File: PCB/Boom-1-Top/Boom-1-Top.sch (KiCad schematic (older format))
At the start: 983 parts, among them J1 DEBUG, J10 PIC_DEBUG, J11 PIC_DEBUG, J12 PIC_DEBUG, J13 PIC_DEBUG, J14 PIC_DEBUG, J15 USB_B_Micro, J16 SD_Card, J17 BT_DEBUG, J18 12V Supply, J19 3V3 Bypass, J2 MIDI IN, J20 5V Bypass, J21 Env +12V Supply, J22 Env -12V Supply, J23 OLEDConn, J3 MIDI OUT, J37 Osc1Conn, J38 Osc2Conn, J39 SubNoiseConn, J4 PIC_DEBUG, J40 FiltConn2, J41 EnvGenConn2, J42 EnvGenConn1, J43 FXConn1, J44 FiltConn1, J45 FXConn2, J46 EnvGenConn3, J5 PIC_DEBUG, J6 PIC_DEBUG, J7 PIC_DEBUG, J8 PIC_DEBUG, J9 PIC_DEBUG, Q1 AO3401A, Q2 AO3401A, SW1 Osc1SawEncoder, SW10 SubToOsc2FiltEncoder, SW11 Osc1ToOsc2FiltEncoder, SW12 Osc1FiltFreqEncoder, SW13 Osc2FiltFreqEncoder, SW14 SubFiltFreqEncoder, SW15 OscFiltEnvAttackEncoder, SW16 SubFiltEnvAttackEncoder, SW17 Osc1FiltResEncoder, SW18 Osc2FiltResEncoder, SW19 SubFiltResEncoder, SW2 Osc1SqrEncoder, SW20 OscFiltEnvDecayEncoder, SW21 SubFiltEnvDecayEncoder, SW22 OscFiltEnvSustainEncoder, SW23 SubFiltEnvSustainEncoder, SW24 Osc1DriveEncoder, SW25 Osc2DistortionEncoder, SW26 OscFiltEnvReleaseEncoder, SW27 SubFiltEnvReleaseEncoder, SW28 FXWetDryEncoder, SW29 SubAmpEnvAttackEncoder, SW3 Rotary_Encoder, SW30 OscAmpEnvAttackEncoder, SW31 FXControl1Encoder, SW32 SubAmpEnvDecayEncoder, SW33 OscAmpEnvDecayEncoder, SW34 FXControl2Encoder, SW35 SubAmpEnvSustainEncoder, SW36 OscAmpEnvSustainEncoder, SW37 FXControl3Encoder, SW38 FXFeedbackEncoder, SW39 SubAmpEnvReleaseEncoder, SW4 Rotary_Encoder_Switch, SW40 OscAmpEnvReleaseEncoder, SW41 Reset, SW42 SW_Push, SW43 Reset, SW44 SW_Push, SW45 SW_Push, SW46 SW_Push, SW47 SW_Push, SW48 SW_Push, SW49 SW_Push, SW5 Rotary_Encoder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

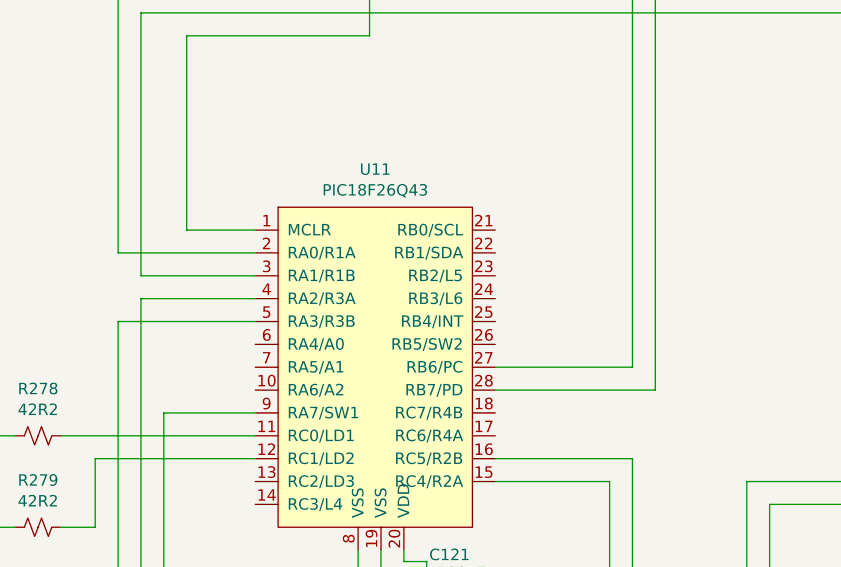
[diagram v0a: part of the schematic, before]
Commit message: U11 PIC i2c
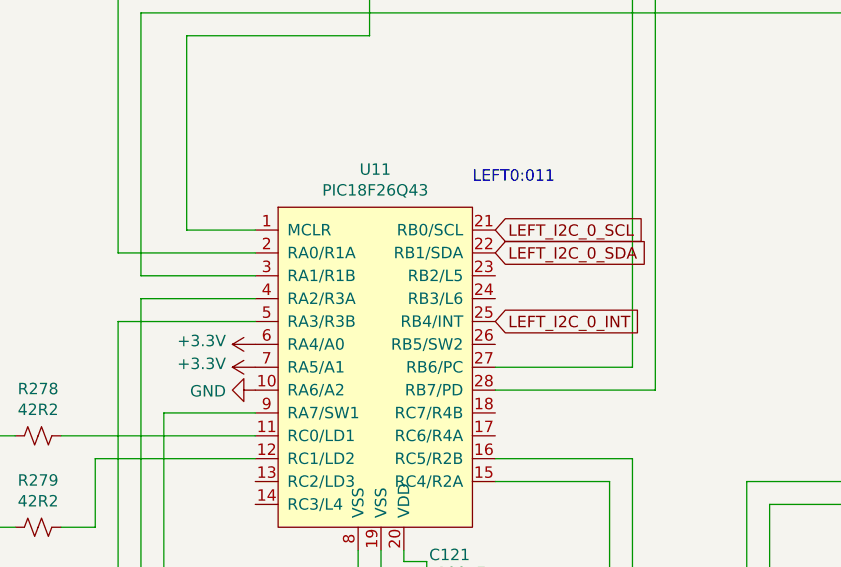
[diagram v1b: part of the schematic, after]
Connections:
- net +3V3: now also U11.6 (RA4/A0), U11.7 (RA5/A1)
- net GND: now also U11.10 (RA6/A2)
- net LEFT_I2C_0_INT: now also U11.25 (RB4/INT)
- net LEFT_I2C_0_SCL: now also U11.21 (RB0/SCL)
- net LEFT_I2C_0_SDA: now also U11.22 (RB1/SDA)
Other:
- note added: "LEFT0:011"
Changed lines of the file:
@@
 LEFT_I2C_2_SCL
 $Comp
-L power:GND #PWR?
+L power:GND #PWR0914
 U 1 1 63216B9C
 P 37600 22500
-F 0 "#PWR?" H 37600 22250 50  0001 C CNN
+F 0 "#PWR0914" H 37600 22250 50  0001 C CNN
 F 1 "GND" V 37605 22372 50  0000 R CNN
 F 2 "" H 37600 22500 50  0001 C CNN
@@
 Wire Wire Line
 	37600 22600 37600 22700
+Text Notes 28650 16100 0    50   ~ 0
+LEFT0:011
+Text GLabel 28750 16700 2    50   Input ~ 0
+LEFT_I2C_0_INT
+Text GLabel 28750 16400 2    50   Input ~ 0
+LEFT_I2C_0_SDA
+Text GLabel 28750 16300 2    50   Input ~ 0
+LEFT_I2C_0_SCL
+$Comp
+L power:+3.3V #PWR?
+U 1 1 63C71E16
+P 27700 16800
+F 0 "#PWR?" H 27700 16650 50  0001 C CNN
+F 1 "+3.3V" V 27715 16928 50  0000 L CNN
+F 2 "" H 27700 16800 50  0001 C CNN
+F 3 "" H 27700 16800 50  0001 C CNN
+	1    27700 16800
+	0    -1   -1   0
+$EndComp
+$Comp
+L power:+3.3V #PWR?
+U 1 1 63C726CC
+P 27700 16900
+F 0 "#PWR?" H 27700 16750 50  0001 C CNN
+F 1 "+3.3V" V 27715 17028 50  0000 L CNN
+F 2 "" H 27700 16900 50  0001 C CNN
+F 3 "" H 27700 16900 50  0001 C CNN
+	1    27700 16900
+	0    -1   -1   0
+$EndComp
+$Comp
+L power:GND #PWR?
+U 1 1 63C7E3D9
+P 27700 17000
+F 0 "#PWR?" H 27700 16750 50  0001 C CNN
+F 1 "GND" V 27705 16872 50  0000 R CNN
+F 2 "" H 27700 17000 50  0001 C CNN
+F 3 "" H 27700 17000 50  0001 C CNN
+	1    27700 17000
+	0    1    1    0
+$EndComp
 $EndSCHEMATC

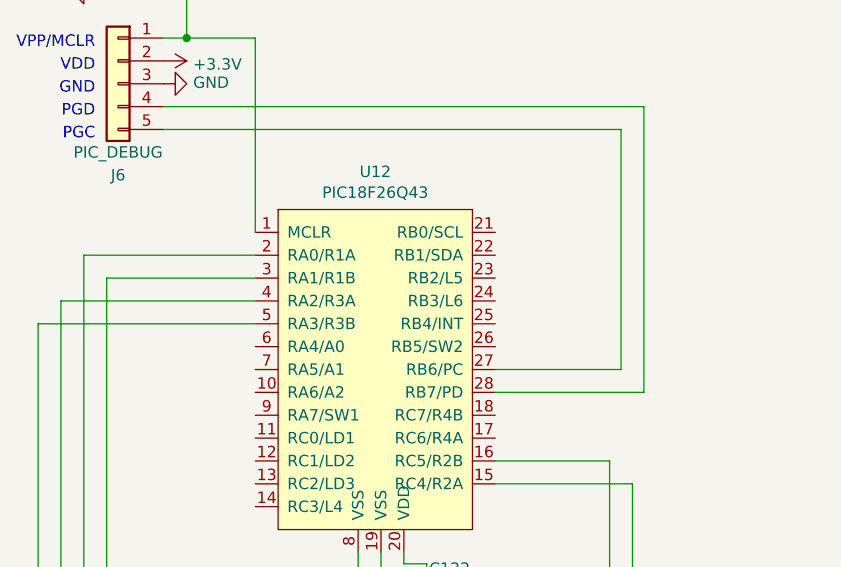
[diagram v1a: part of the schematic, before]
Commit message: U12 PIC i2c
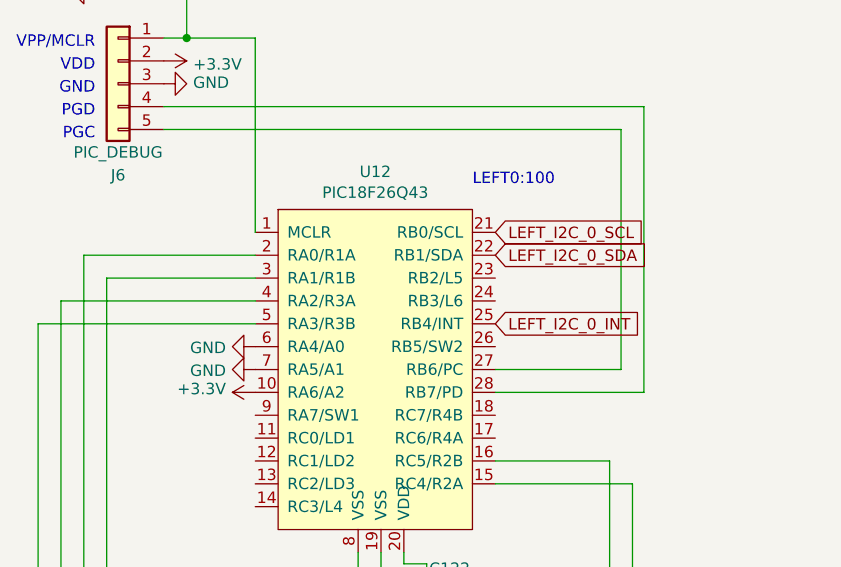
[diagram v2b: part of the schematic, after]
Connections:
- net +3V3: now also U12.10 (RA6/A2)
- net GND: now also U12.6 (RA4/A0), U12.7 (RA5/A1)
- net LEFT_I2C_0_INT: now also U12.25 (RB4/INT)
- net LEFT_I2C_0_SCL: now also U12.21 (RB0/SCL)
- net LEFT_I2C_0_SDA: now also U12.22 (RB1/SDA)
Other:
- note added: "LEFT0:100"
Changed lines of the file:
@@
 LEFT_I2C_0_SCL
 $Comp
-L power:+3.3V #PWR?
+L power:+3.3V #PWR0915
 U 1 1 63C71E16
 P 27700 16800
-F 0 "#PWR?" H 27700 16650 50  0001 C CNN
+F 0 "#PWR0915" H 27700 16650 50  0001 C CNN
 F 1 "+3.3V" V 27715 16928 50  0000 L CNN
 F 2 "" H 27700 16800 50  0001 C CNN
@@
 $EndComp
 $Comp
-L power:+3.3V #PWR?
+L power:+3.3V #PWR0916
 U 1 1 63C726CC
 P 27700 16900
-F 0 "#PWR?" H 27700 16750 50  0001 C CNN
+F 0 "#PWR0916" H 27700 16750 50  0001 C CNN
 F 1 "+3.3V" V 27715 17028 50  0000 L CNN
 F 2 "" H 27700 16900 50  0001 C CNN
@@
 $EndComp
 $Comp
-L power:GND #PWR?
+L power:GND #PWR0917
 U 1 1 63C7E3D9
 P 27700 17000
-F 0 "#PWR?" H 27700 16750 50  0001 C CNN
+F 0 "#PWR0917" H 27700 16750 50  0001 C CNN
 F 1 "GND" V 27705 16872 50  0000 R CNN
 F 2 "" H 27700 17000 50  0001 C CNN
@@
 	0    1    1    0
 $EndComp
+Text Notes 30750 23250 0    50   ~ 0
+LEFT0:100
+Text GLabel 30850 23850 2    50   Input ~ 0
+LEFT_I2C_0_INT
+Text GLabel 30850 23550 2    50   Input ~ 0
+LEFT_I2C_0_SDA
+Text GLabel 30850 23450 2    50   Input ~ 0
+LEFT_I2C_0_SCL
+$Comp
+L power:+3.3V #PWR?
+U 1 1 64270E6A
+P 29800 24150
+F 0 "#PWR?" H 29800 24000 50  0001 C CNN
+F 1 "+3.3V" V 29815 24278 50  0000 L CNN
+F 2 "" H 29800 24150 50  0001 C CNN
+F 3 "" H 29800 24150 50  0001 C CNN
+	1    29800 24150
+	0    -1   -1   0
+$EndComp
+$Comp
+L power:GND #PWR?
+U 1 1 6427D376
+P 29800 23950
+F 0 "#PWR?" H 29800 23700 50  0001 C CNN
+F 1 "GND" V 29805 23822 50  0000 R CNN
+F 2 "" H 29800 23950 50  0001 C CNN
+F 3 "" H 29800 23950 50  0001 C CNN
+	1    29800 23950
+	0    1    1    0
+$EndComp
+$Comp
+L power:GND #PWR?
+U 1 1 6427D96E
+P 29800 24050
+F 0 "#PWR?" H 29800 23800 50  0001 C CNN
+F 1 "GND" V 29805 23922 50  0000 R CNN
+F 2 "" H 29800 24050 50  0001 C CNN
+F 3 "" H 29800 24050 50  0001 C CNN
+	1    29800 24050
+	0    1    1    0
+$EndComp

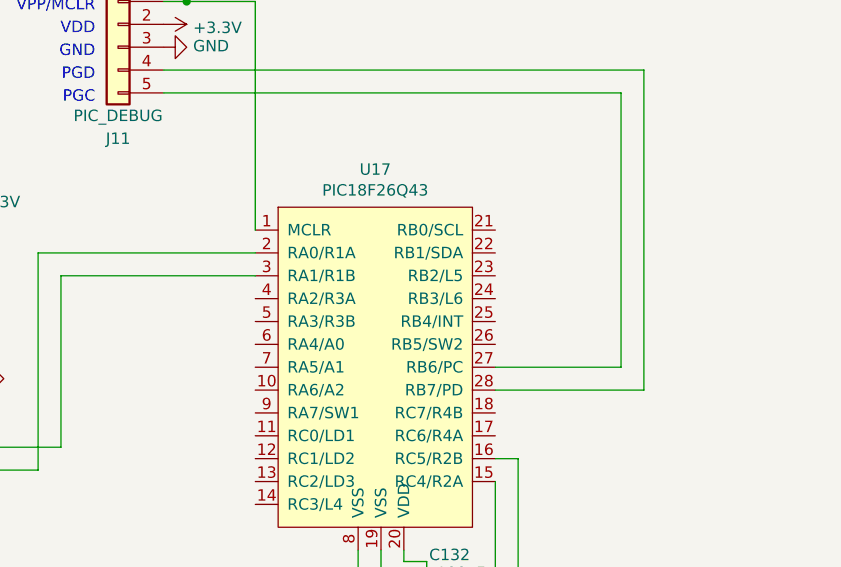
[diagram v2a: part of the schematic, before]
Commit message: U17 PIC i2c
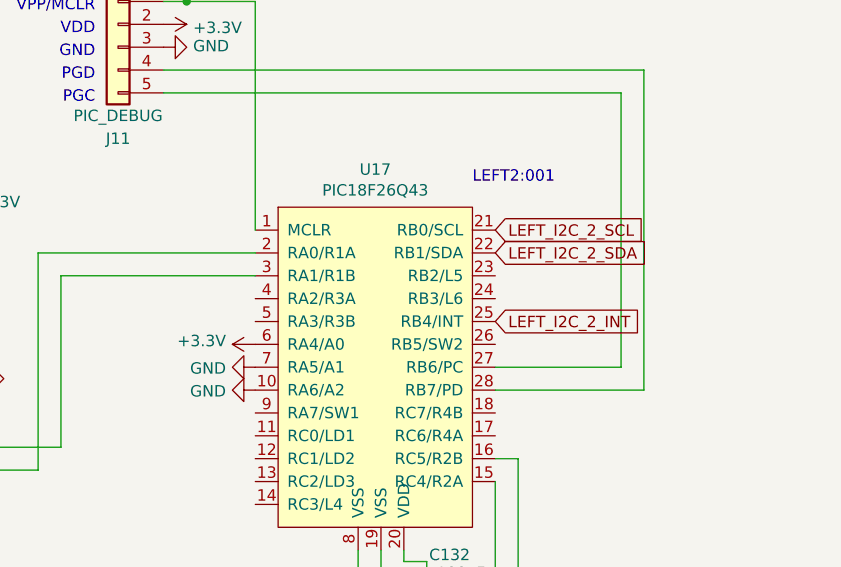
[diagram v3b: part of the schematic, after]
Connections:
- net +3V3: now also U17.6 (RA4/A0)
- net GND: now also U17.10 (RA6/A2), U17.7 (RA5/A1)
- net LEFT_I2C_2_INT: now also U17.25 (RB4/INT)
- net LEFT_I2C_2_SCL: now also U17.21 (RB0/SCL)
- net LEFT_I2C_2_SDA: now also U17.22 (RB1/SDA)
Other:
- note added: "LEFT2:001"
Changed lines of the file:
@@
 LEFT_I2C_0_SCL
 $Comp
-L power:+3.3V #PWR?
+L power:+3.3V #PWR0918
 U 1 1 64270E6A
 P 29800 24150
-F 0 "#PWR?" H 29800 24000 50  0001 C CNN
+F 0 "#PWR0918" H 29800 24000 50  0001 C CNN
 F 1 "+3.3V" V 29815 24278 50  0000 L CNN
 F 2 "" H 29800 24150 50  0001 C CNN
@@
 $EndComp
 $Comp
-L power:GND #PWR?
+L power:GND #PWR0919
 U 1 1 6427D376
 P 29800 23950
-F 0 "#PWR?" H 29800 23700 50  0001 C CNN
+F 0 "#PWR0919" H 29800 23700 50  0001 C CNN
 F 1 "GND" V 29805 23822 50  0000 R CNN
 F 2 "" H 29800 23950 50  0001 C CNN
@@
 $EndComp
 $Comp
-L power:GND #PWR?
+L power:GND #PWR0920
 U 1 1 6427D96E
 P 29800 24050
-F 0 "#PWR?" H 29800 23800 50  0001 C CNN
+F 0 "#PWR0920" H 29800 23800 50  0001 C CNN
 F 1 "GND" V 29805 23922 50  0000 R CNN
 F 2 "" H 29800 24050 50  0001 C CNN
@@
 	0    1    1    0
 $EndComp
+Text Notes 39250 28900 0    50   ~ 0
+LEFT2:001
+Text GLabel 39350 29500 2    50   Input ~ 0
+LEFT_I2C_2_INT
+Text GLabel 39350 29200 2    50   Input ~ 0
+LEFT_I2C_2_SDA
+Text GLabel 39350 29100 2    50   Input ~ 0
+LEFT_I2C_2_SCL
+$Comp
+L power:+3.3V #PWR?
+U 1 1 647A28C1
+P 38300 29600
+F 0 "#PWR?" H 38300 29450 50  0001 C CNN
+F 1 "+3.3V" V 38315 29728 50  0000 L CNN
+F 2 "" H 38300 29600 50  0001 C CNN
+F 3 "" H 38300 29600 50  0001 C CNN
+	1    38300 29600
+	0    -1   -1   0
+$EndComp
+$Comp
+L power:GND #PWR?
+U 1 1 647AECBB
+P 38300 29700
+F 0 "#PWR?" H 38300 29450 50  0001 C CNN
+F 1 "GND" V 38305 29572 50  0000 R CNN
+F 2 "" H 38300 29700 50  0001 C CNN
+F 3 "" H 38300 29700 50  0001 C CNN
+	1    38300 29700
+	0    1    1    0
+$EndComp
+$Comp
+L power:GND #PWR?
+U 1 1 647AED7E
+P 38300 29800
+F 0 "#PWR?" H 38300 29550 50  0001 C CNN
+F 1 "GND" V 38305 29672 50  0000 R CNN
+F 2 "" H 38300 29800 50  0001 C CNN
+F 3 "" H 38300 29800 50  0001 C CNN
+	1    38300 29800
+	0    1    1    0
+$EndComp

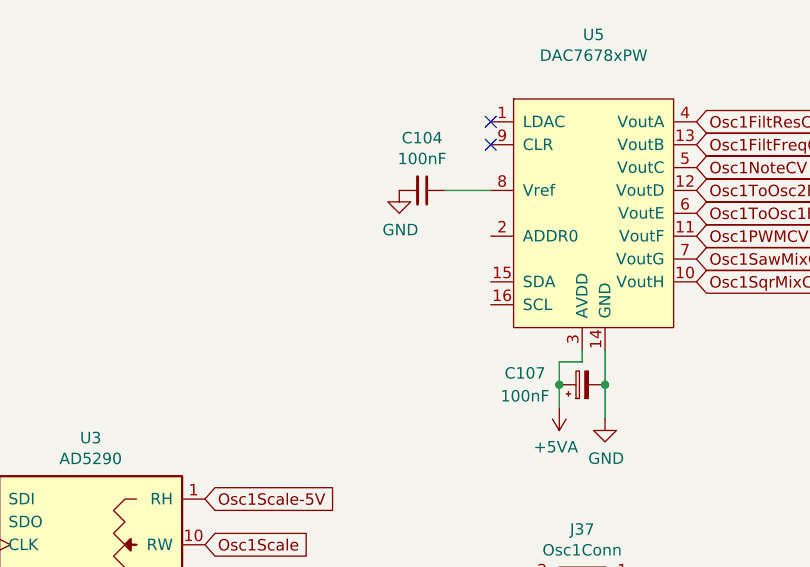
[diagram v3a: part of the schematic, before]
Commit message: U5 DAC i2c
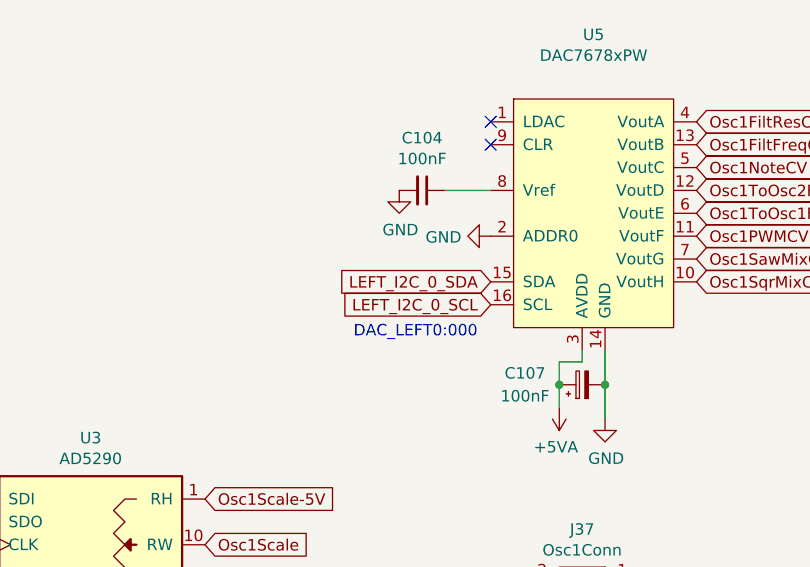
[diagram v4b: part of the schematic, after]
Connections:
- net GND: now also U5.2 (ADDR0)
- net LEFT_I2C_0_SCL: now also U5.16 (SCL)
- net LEFT_I2C_0_SDA: now also U5.15 (SDA)
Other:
- note added: "DAC_LEFT0:000"
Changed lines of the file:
@@
+	0    1    1    0
+$EndComp
+Text Notes 28900 37450 0    50   ~ 0
+DAC_LEFT0:000
+Text GLabel 29500 37200 0    50   Input ~ 0
+LEFT_I2C_0_SDA
+Text GLabel 29500 37300 0    50   Input ~ 0
+LEFT_I2C_0_SCL
+$Comp
+L power:GND #PWR?
+U 1 1 612870A5
+P 29500 37000
+F 0 "#PWR?" H 29500 36750 50  0001 C CNN
+F 1 "GND" V 29505 36872 50  0000 R CNN
+F 2 "" H 29500 37000 50  0001 C CNN
+F 3 "" H 29500 37000 50  0001 C CNN
+	1    29500 37000
 	0    1    1    0
 $EndComp

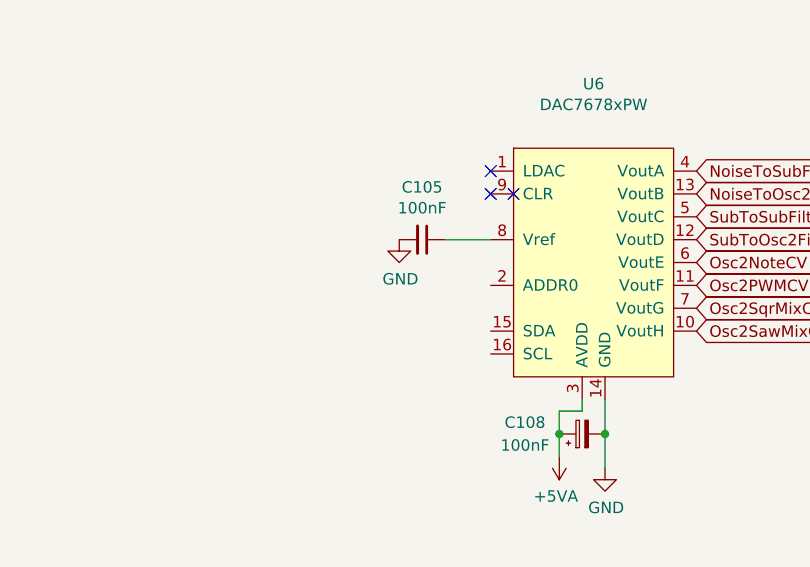
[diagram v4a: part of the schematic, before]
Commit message: U6 DAC i2c
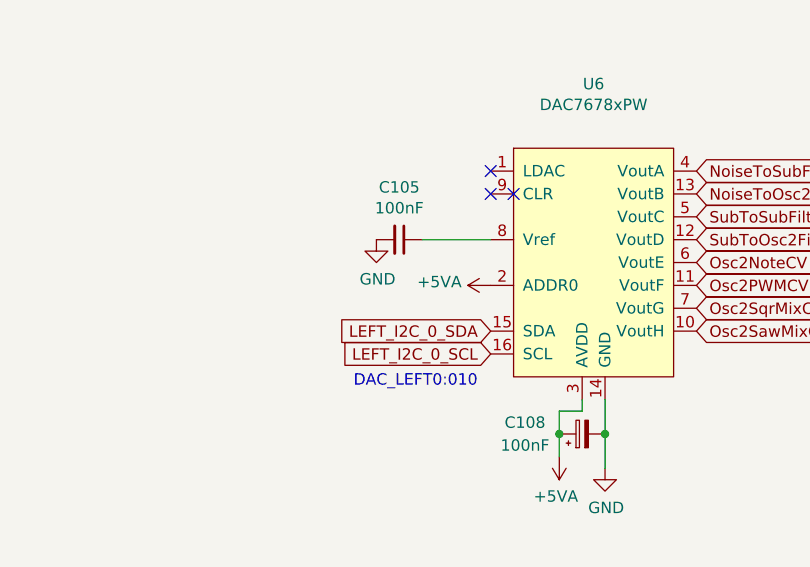
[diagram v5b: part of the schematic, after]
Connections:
- net +5VA: now also U6.2 (ADDR0)
- net LEFT_I2C_0_SCL: now also U6.16 (SCL)
- net LEFT_I2C_0_SDA: now also U6.15 (SDA)
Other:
- note added: "DAC_LEFT0:010"
- moved on the sheet: C105
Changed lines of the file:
@@
 L Device:C_Small C105
 U 1 1 5FE083BC
-P 29200 43200
-F 0 "C105" V 28971 43200 50  0000 C CNN
-F 1 "100nF" V 29062 43200 50  0000 C CNN
-F 2 "Capacitor_SMD:C_0402_1005Metric" H 29200 43200 50  0001 C CNN
-F 3 "~" H 29200 43200 50  0001 C CNN
-	1    29200 43200
+P 29100 43200
+F 0 "C105" V 28871 43200 50  0000 C CNN
+F 1 "100nF" V 28962 43200 50  0000 C CNN
+F 2 "Capacitor_SMD:C_0402_1005Metric" H 29100 43200 50  0001 C CNN
+F 3 "~" H 29100 43200 50  0001 C CNN
+	1    29100 43200
 	0    1    1    0
 $EndComp
@@
 L power:GND #PWR0279
 U 1 1 5FE0C246
-P 29100 43200
-F 0 "#PWR0279" H 29100 42950 50  0001 C CNN
-F 1 "GND" H 29105 43027 50  0000 C CNN
-F 2 "" H 29100 43200 50  0001 C CNN
-F 3 "" H 29100 43200 50  0001 C CNN
-	1    29100 43200
+P 29000 43200
+F 0 "#PWR0279" H 29000 42950 50  0001 C CNN
+F 1 "GND" H 29005 43027 50  0000 C CNN
+F 2 "" H 29000 43200 50  0001 C CNN
+F 3 "" H 29000 43200 50  0001 C CNN
+	1    29000 43200
 	1    0    0    -1
 $EndComp
 Wire Wire Line
-	29300 43200 29500 43200
+	29200 43200 29500 43200
 $Comp
 L Device:C_Small C109
@@
 LEFT_I2C_2_SCL
 $Comp
-L power:+3.3V #PWR?
+L power:+3.3V #PWR0921
 U 1 1 647A28C1
 P 38300 29600
-F 0 "#PWR?" H 38300 29450 50  0001 C CNN
+F 0 "#PWR0921" H 38300 29450 50  0001 C CNN
 F 1 "+3.3V" V 38315 29728 50  0000 L CNN
 F 2 "" H 38300 29600 50  0001 C CNN
@@
 $EndComp
 $Comp
-L power:GND #PWR?
+L power:GND #PWR0922
 U 1 1 647AECBB
 P 38300 29700
-F 0 "#PWR?" H 38300 29450 50  0001 C CNN
+F 0 "#PWR0922" H 38300 29450 50  0001 C CNN
 F 1 "GND" V 38305 29572 50  0000 R CNN
 F 2 "" H 38300 29700 50  0001 C CNN
@@
 $EndComp
 $Comp
-L power:GND #PWR?
+L power:GND #PWR0923
 U 1 1 647AED7E
 P 38300 29800
-F 0 "#PWR?" H 38300 29550 50  0001 C CNN
+F 0 "#PWR0923" H 38300 29550 50  0001 C CNN
 F 1 "GND" V 38305 29672 50  0000 R CNN
 F 2 "" H 38300 29800 50  0001 C CNN
@@
 LEFT_I2C_0_SCL
 $Comp
-L power:GND #PWR?
+L power:GND #PWR0924
 U 1 1 612870A5
 P 29500 37000
-F 0 "#PWR?" H 29500 36750 50  0001 C CNN
+F 0 "#PWR0924" H 29500 36750 50  0001 C CNN
 F 1 "GND" V 29505 36872 50  0000 R CNN
 F 2 "" H 29500 37000 50  0001 C CNN
@@
 	0    1    1    0
 $EndComp
+Text Notes 28900 43850 0    50   ~ 0
+DAC_LEFT0:010
+Text GLabel 29500 43600 0    50   Input ~ 0
+LEFT_I2C_0_SDA
+Text GLabel 29500 43700 0    50   Input ~ 0
+LEFT_I2C_0_SCL
+$Comp
+L power:+5VA #PWR?
+U 1 1 61BE5A1B
+P 29500 43400
+F 0 "#PWR?" H 29500 43250 50  0001 C CNN
+F 1 "+5VA" V 29515 43527 50  0000 L CNN
+F 2 "" H 29500 43400 50  0001 C CNN
+F 3 "" H 29500 43400 50  0001 C CNN
+	1    29500 43400
+	0    -1   -1   0
+$EndComp
 $EndSCHEMATC

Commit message: U7 DAC i2c
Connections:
- net GND: now also U7.2 (ADDR0)
- net LEFT_I2C_2_SCL: now also U7.16 (SCL)
- net LEFT_I2C_2_SDA: now also U7.15 (SDA)
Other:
- note added: "DAC_LEFT2:000"
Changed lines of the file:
@@
 LEFT_I2C_0_SCL
 $Comp
-L power:+5VA #PWR?
+L power:+5VA #PWR0925
 U 1 1 61BE5A1B
 P 29500 43400
-F 0 "#PWR?" H 29500 43250 50  0001 C CNN
+F 0 "#PWR0925" H 29500 43250 50  0001 C CNN
 F 1 "+5VA" V 29515 43527 50  0000 L CNN
 F 2 "" H 29500 43400 50  0001 C CNN
@@
 	0    -1   -1   0
 $EndComp
+Text Notes 32900 40050 0    50   ~ 0
+DAC_LEFT2:000
+Text GLabel 33500 39800 0    50   Input ~ 0
+LEFT_I2C_2_SDA
+Text GLabel 33500 39900 0    50   Input ~ 0
+LEFT_I2C_2_SCL
+$Comp
+L power:GND #PWR?
+U 1 1 626D0E19
+P 33500 39600
+F 0 "#PWR?" H 33500 39350 50  0001 C CNN
+F 1 "GND" V 33505 39472 50  0000 R CNN
+F 2 "" H 33500 39600 50  0001 C CNN
+F 3 "" H 33500 39600 50  0001 C CNN
+	1    33500 39600
+	0    1    1    0
+$EndComp
 $EndSCHEMATC
